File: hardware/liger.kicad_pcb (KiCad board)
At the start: 2 copper layers, 33.1 x 92.2 mm, 56 parts, among them J1 Conn_02x08_Odd_Even, Q1 Q_NPN_BEC, Q4 PMOS-DMG3413L, U1 ESP-WROOM-32, U10 EKMC1601112, U12 soft-button-4x, U2 IR-RX-TSOP34438, U3 SPH0645LM4H-B, U4 MCP73831T, U5 MAX98357AETE+T, U6 SI7020-A20, U8 TSL45315CL, U9 AP2112

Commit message: update
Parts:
- C10, C11, C5, C6, C7, C8, C9, D3, D6, Q4, R10, R11, R17, R19, R22, R9, U1, U4, U5, U9: moved to B.Cu
- moved C2 253.4 mm to (135.1, 157.5)
- moved C3 253.4 mm to (135.1, 156.0)
- moved C1 253.4 mm to (131.8, 156.0)
- moved C4 253.4 mm to (131.8, 157.5)
- moved R1 253.4 mm to (135.1, 154.5)
- moved R2 253.4 mm to (131.8, 154.5)
- moved R7 253.4 mm to (138.5, 154.5)
- moved R18 230.9 mm to (151.1, 171.9)
- moved R20 230.9 mm to (151.1, 170.4)
- moved R6 230.9 mm to (140.0, 165.1)
- moved D3 206.2 mm to (160.7, 121.6)
- moved C12 203.1 mm to (133.3, 172.1)
- moved D2 203.1 mm to (125.5, 175.8)
- moved D4 203.1 mm to (123.3, 177.4)
- moved D5 203.1 mm to (122.1, 175.8)
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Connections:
- U5 pad 10: Net-(LS1-Pad2) -> Net-(LS1-Pad1)
- U5 pad 9: Net-(LS1-Pad1) -> Net-(LS1-Pad2)
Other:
- board text added: "room sensor v0.7"
- board text removed: "room sensor v0.6"

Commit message: layout complete
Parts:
- C1, C2, C3, C4, Q1, R1, R18, R2, R20, R26, R3, R4, R5, R6, R7: moved to B.Cu
- moved R6 106.2 mm to (132.1, 59.1), turned to 270 degrees
- moved R18 104.2 mm to (147.0, 67.9), turned to 180 degrees
- moved R20 101.0 mm to (146.9, 69.5)
- moved R3 99.4 mm to (158.0, 60.7)
- moved R2 95.4 mm to (137.4, 59.2), turned to 270 degrees
- moved R5 92.6 mm to (159.3, 69.1), turned to 180 degrees
- moved R4 91.6 mm to (152.9, 68.3), turned to 90 degrees
- moved Q1 91.5 mm to (155.7, 68.3)
- moved C1 89.4 mm to (159.4, 71.0), turned to 180 degrees
- moved C2 88.3 mm to (159.4, 72.6), turned to 180 degrees
- moved C4 86.2 mm to (159.4, 75.8), turned to 180 degrees
- moved C3 85.3 mm to (159.4, 74.2), turned to 180 degrees
- moved R23 82.0 mm to (134.4, 99.4), turned to 180 degrees
- moved R26 79.3 mm to (139.8, 100.7), turned to 180 degrees
- moved D4 74.4 mm to (135.6, 104.0), turned to 270 degrees
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
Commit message: corrections
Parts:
- C12, R14, R15, R16, R23: moved to B.Cu
- moved R16 6.39 mm to (137.9, 116.5)
- moved R15 6.35 mm to (137.9, 108.8)
- moved D5 5.48 mm to (137.9, 116.5)
- moved D4 5.35 mm to (137.9, 108.8)
- moved D2 5.32 mm to (156.5, 112.9)
- moved R14 3.82 mm to (156.5, 116.7), turned to 270 degrees
- moved C12 0.62 mm to (134.1, 101.6), turned to 0 degrees
- moved U12 0.61 mm to (146.7, 88.4)
- moved R23 0.58 mm to (134.1, 99.9), turned to 0 degrees

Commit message: ws2812b
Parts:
- removed R23: R_150, Resistor_SMD:R_0603_1608Metric_Pad1.05x0.95mm_HandSolder
- added LOGO: , open-automation:pyfi_symbol, B.Cu at (163.1, 49.8)
- D7: value WS2812 -> WS2812B; footprint LED_SMD:LED_WS2812_PLCC6_5.0x5.0mm_P1.6mm -> LED_SMD:LED_WS2812B_PLCC4_5.0x5.0mm_P3.2mm
- moved C12 25.1 mm to (159.1, 100.3), turned to 180 degrees
- moved R14 0.97 mm to (157.4, 117.1), turned to 0 degrees
- moved R3 0.51 mm to (158.0, 61.2)
- moved D7 0.09 mm to (147.1, 88.6), turned to 180 degrees
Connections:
- C12 pad 2: Net-(C12-Pad2) -> /V_USB
- D7 pad 1: Net-(D7-Pad1) -> /V_USB
- D7 pad 2: /BUTTON_LED -> Net-(D7-Pad2)
- D7 pad 3: Net-(C12-Pad2) -> GND
- D7 pad 4: Net-(D7-Pad4) -> /BUTTON_LED

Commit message: pcb complete
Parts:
- moved D3 4.48 mm to (160.9, 117.1)
- moved R19 1.26 mm to (159.5, 107.4), turned to 270 degrees
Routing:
- net /3V3: track 0.00 -> 165.5 mm, vias 0 -> 14
- net /I2S_BCLK: track 0.00 -> 126.8 mm, vias 0 -> 5
- net /SCL: track 0.00 -> 83.8 mm, vias 0 -> 2
- net /SDA: track 0.00 -> 76.3 mm, vias 0 -> 2
- net /I2S_WS: track 0.00 -> 73.3 mm, vias 0 -> 7
- net /ZERO_DETECT: track 0.00 -> 62.1 mm, vias 0 -> 8
- net /V_USB: track 0.00 -> 56.1 mm, vias 0 -> 3
- net /TXD: track 0.00 -> 54.6 mm, vias 0 -> 4
- net /RXD: track 0.00 -> 53.6 mm, vias 0 -> 4
- net /IR_RX: track 0.00 -> 50.8 mm, vias 0 -> 8
- net /I2S_DATA_OUT: track 0.00 -> 46.4 mm, vias 0 -> 10
- net GND: track 0.00 -> 43.4 mm, vias 0 -> 27
- net /IR_TX: track 0.00 -> 41.9 mm, vias 0 -> 6
- net /PROG: track 0.00 -> 38.2 mm, vias 0 -> 4
- net /RELAY: track 0.00 -> 34.1 mm, vias 0 -> 7
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
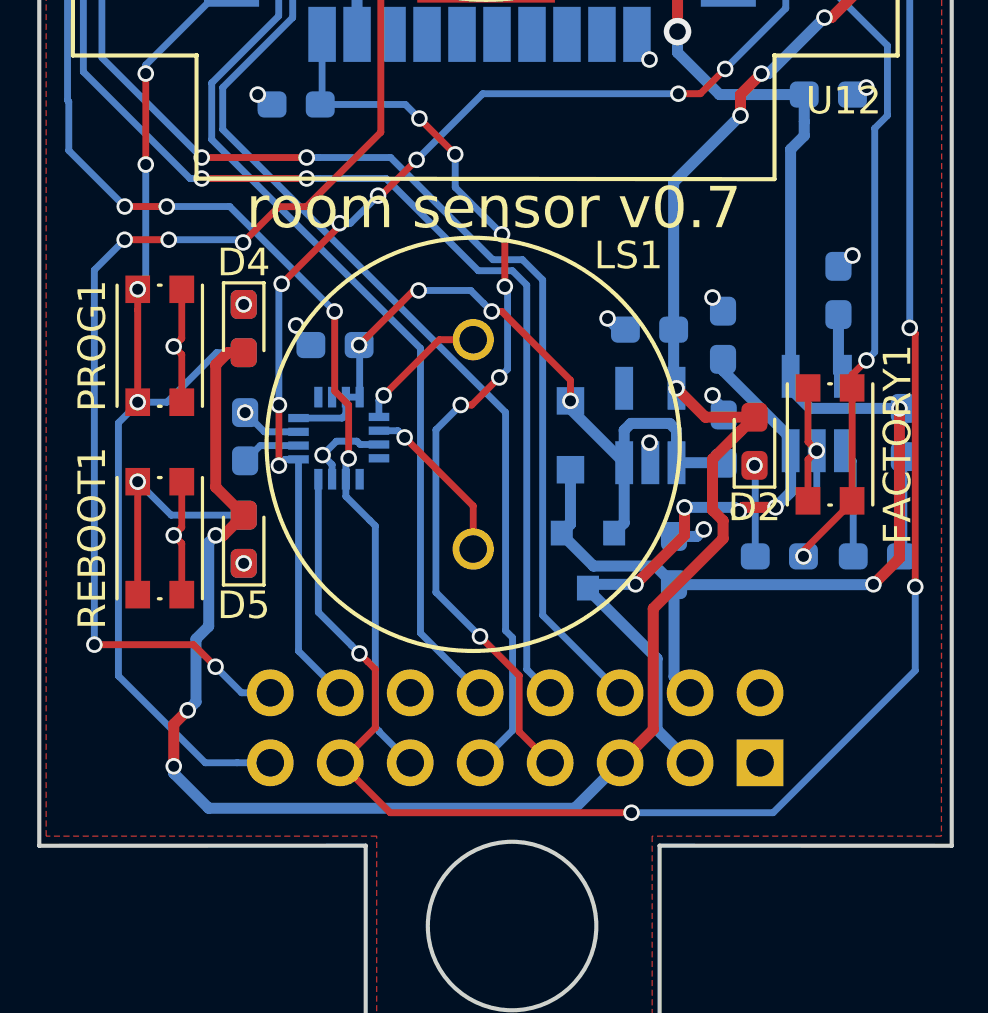
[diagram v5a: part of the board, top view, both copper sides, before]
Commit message: final touches on silkscreen, sending off to oshpark
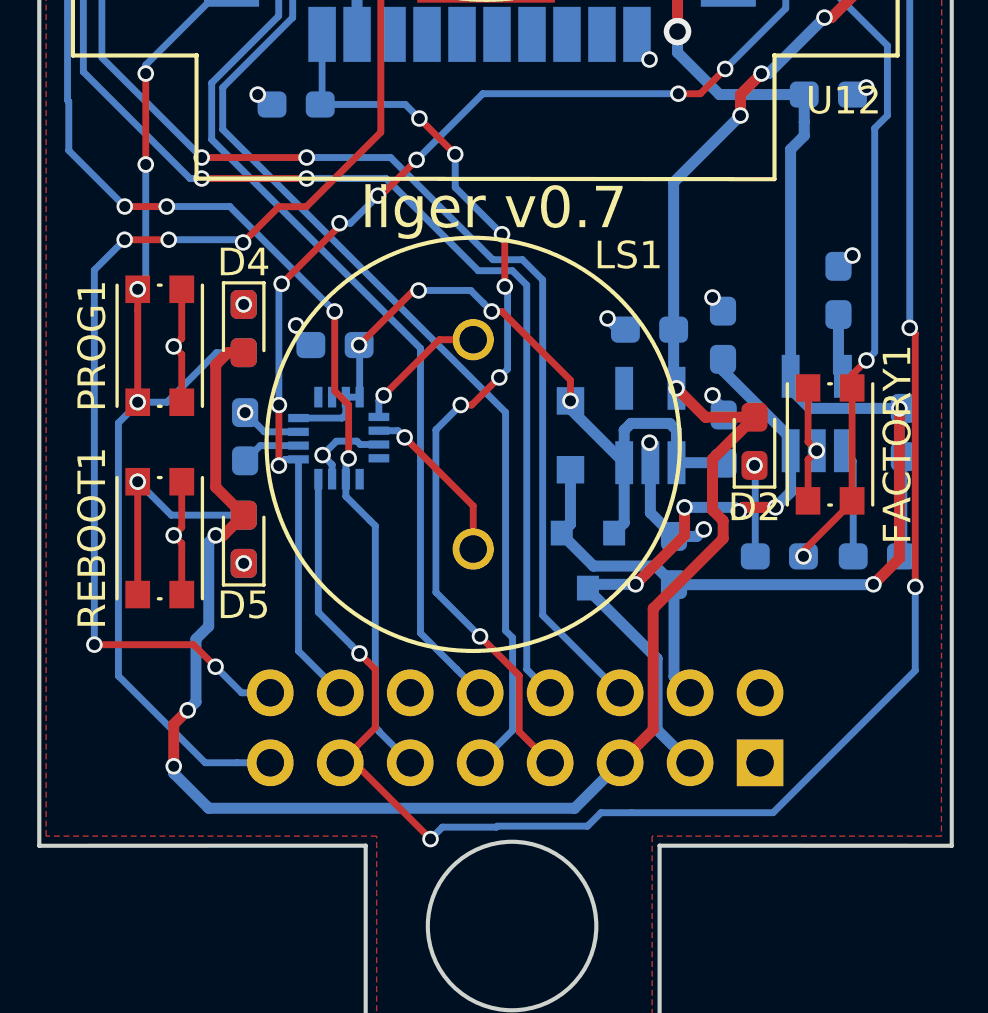
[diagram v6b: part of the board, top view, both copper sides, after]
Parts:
- moved LOGO 3.22 mm to (159.9, 50.3)
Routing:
- net GND: track 43.4 -> 44.5 mm
- net /I2S_BCLK: track 126.8 -> 127.7 mm
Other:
- board text added: "liger v0.7"
- board text removed: "room sensor v0.7"
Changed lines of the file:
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@@
-(kicad_pcb (version 20171130) (host pcbnew 5.0.0-rc3-unknown-3df2743~65~ubuntu17.10.1)
+(kicad_pcb (version 20171130) (host pcbnew 6.0.0-rc1-unknown-7a10feb~66~ubuntu18.04.1)
   (general
     (thickness 1.6)
     (drawings 57)
-    (tracks 716)
+    (tracks 723)
     (zones 0)
     (modules 56)
@@
   )
   (setup
-    (last_trace_width 0.25)
+    (last_trace_width 0.4)
     (user_trace_width 0.25)
     (user_trace_width 0.4)
@@
     (zone_45_only yes)
     (trace_min 0.2)
-    (segment_width 0.2)
-    (edge_width 0.15)
     (via_size 0.6)
     (via_drill 0.4)
@@
     (uvia_min_size 0.2)
     (uvia_min_drill 0.1)
+    (edge_width 0.15)
+    (segment_width 0.2)
     (pcb_text_width 0.3)
     (pcb_text_size 1.5 1.5)
@@
     (visible_elements FFFFFF7F)
     (pcbplotparams
-      (layerselection 0x010f0_80000001)
+      (layerselection 0x010f0_ffffffff)
       (usegerberextensions false)
       (usegerberattributes false)
@@
   )
   (module open-automation:pyfi_symbol (layer B.Cu)
-    (at 163.068 49.784 180)
+    (at 159.893 50.3428 180)
     (fp_text reference LOGO (at 0 -5 180) (layer B.SilkS) hide
       (effects (font (size 1.524 1.524) (thickness 0.3)) (justify mirror))
@@
   (gr_line (start 427.228 142.748) (end 394.2715 75.7555) (layer Dwgs.User) (width 0.15))
   (gr_line (start 427.2915 75.7555) (end 394.2715 142.748) (layer Dwgs.User) (width 0.15))
-  (gr_text "room sensor v0.7" (at 147 104.45) (layer F.SilkS)
+  (gr_text "liger v0.7" (at 147 104.45) (layer F.SilkS)
     (effects (font (size 1.5 1.5) (thickness 0.3)))
   )
@@
   (segment (start 151.779 108.8644) (end 151.5364 108.8644) (width 0.4) (layer B.Cu) (net 1))
   (segment (start 151.5364 108.8644) (end 151.13 108.458) (width 0.4) (layer B.Cu) (net 1))
-  (segment (start 158.7246 113.2586) (end 158.7246 114.7626) (width 0.25) (layer B.Cu) (net 1))
-  (segment (start 158.7246 114.7626) (end 158.4072 115.08) (width 0.25) (layer B.Cu) (net 1))
   (via (at 158.7246 113.2586) (size 0.6) (drill 0.4) (layers F.Cu B.Cu) (net 1))
   (segment (start 158.4072 110.98) (end 158.4072 112.9412) (width 0.25) (layer F.Cu) (net 1))
   (segment (start 158.4072 112.9412) (end 158.7246 113.2586) (width 0.25) (layer F.Cu) (net 1))
-  (segment (start 158.4072 113.576) (end 158.7246 113.2586) (width 0.25) (layer F.Cu) (net 1))
-  (segment (start 158.4072 115.08) (end 158.4072 113.576) (width 0.25) (layer F.Cu) (net 1))
   (segment (start 154.702 67.376) (end 154.702 67.326) (width 0.4) (layer B.Cu) (net 1))
   (via (at 154.178 66.802) (size 0.6) (drill 0.4) (layers F.Cu B.Cu) (net 1))
@@
   (segment (start 139.82501 108.88781) (end 139.82501 108.712) (width 0.25) (layer B.Cu) (net 1))
   (segment (start 140.3604 109.4232) (end 139.82501 108.88781) (width 0.25) (layer B.Cu) (net 1))
+  (segment (start 152.6832 115.5116) (end 153.543 116.3714) (width 0.4) (layer B.Cu) (net 1))
+  (segment (start 152.6832 113.6942) (end 152.6832 115.5116) (width 0.4) (layer B.Cu) (net 1))
+  (segment (start 158.4072 113.576) (end 158.7246 113.2586) (width 0.25) (layer F.Cu) (net 1))
+  (segment (start 158.4072 115.08) (end 158.4072 113.576) (width 0.25) (layer F.Cu) (net 1))
   (segment (start 156.702 64.0174) (end 156.6926 64.008) (width 0.4) (layer B.Cu) (net 2))
   (segment (start 156.702 68.326) (end 156.702 64.0174) (width 0.4) (layer B.Cu) (net 2))
@@
   (segment (start 142.424989 120.918509) (end 142.12499 120.61851) (width 0.25) (layer F.Cu) (net 39))
   (via (at 142.12499 120.61851) (size 0.6) (drill 0.4) (layers F.Cu B.Cu) (net 39))
-  (via (at 152 126.4) (size 0.6) (drill 0.4) (layers F.Cu B.Cu) (net 39))
-  (segment (start 141.4272 124.587) (end 143.2402 126.4) (width 0.25) (layer F.Cu) (net 39))
-  (segment (start 143.2402 126.4) (end 152 126.4) (width 0.25) (layer F.Cu) (net 39))
-  (via (at 162.3 118.2) (size 0.6) (drill 0.4) (layers F.Cu B.Cu) (net 39))
-  (segment (start 162.3 121.239202) (end 162.3 118.2) (width 0.25) (layer B.Cu) (net 39))
-  (segment (start 152 126.4) (end 157.139202 126.4) (width 0.25) (layer B.Cu) (net 39))
-  (segment (start 157.139202 126.4) (end 162.3 121.239202) (width 0.25) (layer B.Cu) (net 39))
-  (via (at 162.1 108.8) (size 0.6) (drill 0.4) (layers F.Cu B.Cu) (net 39))
-  (segment (start 162.3 118.2) (end 162.3 109) (width 0.25) (layer F.Cu) (net 39))
-  (segment (start 162.3 109) (end 162.1 108.8) (width 0.25) (layer F.Cu) (net 39))
-  (segment (start 162.1 94.83) (end 160.1 92.83) (width 0.25) (layer B.Cu) (net 39))
   (segment (start 162.1 108.8) (end 162.1 94.83) (width 0.25) (layer B.Cu) (net 39))
+  (segment (start 162.1 94.83) (end 160.1 92.83) (width 0.25) (layer B.Cu) (net 39))
+  (segment (start 162.3 109) (end 162.1 108.8) (width 0.25) (layer F.Cu) (net 39))
+  (segment (start 162.3 118.2) (end 162.3 109) (width 0.25) (layer F.Cu) (net 39))
+  (via (at 162.1 108.8) (size 0.6) (drill 0.4) (layers F.Cu B.Cu) (net 39))
+  (segment (start 157.139202 126.4) (end 162.3 121.239202) (width 0.25) (layer B.Cu) (net 39))
+  (segment (start 152 126.4) (end 157.139202 126.4) (width 0.25) (layer B.Cu) (net 39))
+  (segment (start 162.3 121.239202) (end 162.3 118.2) (width 0.25) (layer B.Cu) (net 39))
+  (via (at 162.3 118.2) (size 0.6) (drill 0.4) (layers F.Cu B.Cu) (net 39))
+  (segment (start 152 126.4) (end 150.8918 126.4) (width 0.25) (layer B.Cu) (net 39))
+  (segment (start 150.8918 126.4) (end 150.4038 126.888) (width 0.25) (layer B.Cu) (net 39))
+  (segment (start 141.4272 124.7798) (end 141.4272 124.587) (width 0.25) (layer F.Cu) (net 39))
+  (segment (start 147.1318 126.888) (end 147.096 126.9238) (width 0.25) (layer B.Cu) (net 39))
+  (segment (start 150.4038 126.888) (end 147.1318 126.888) (width 0.25) (layer B.Cu) (net 39))
+  (via (at 144.7038 127.3556) (size 0.6) (drill 0.4) (layers F.Cu B.Cu) (net 39))
+  (segment (start 147.096 126.9238) (end 145.1356 126.9238) (width 0.25) (layer B.Cu) (net 39))
+  (segment (start 145.1356 126.9238) (end 144.7038 127.3556) (width 0.25) (layer B.Cu) (net 39))
+  (segment (start 141.9352 124.587) (end 141.4272 124.587) (width 0.25) (layer F.Cu) (net 39))
+  (segment (start 144.7038 127.3556) (end 141.9352 124.587) (width 0.25) (layer F.Cu) (net 39))
   (segment (start 139.911 120.5308) (end 141.4272 122.047) (width 0.25) (layer B.Cu) (net 40))
   (segment (start 139.911 113.5734) (end 139.911 120.5308) (width 0.25) (layer B.Cu) (net 40))

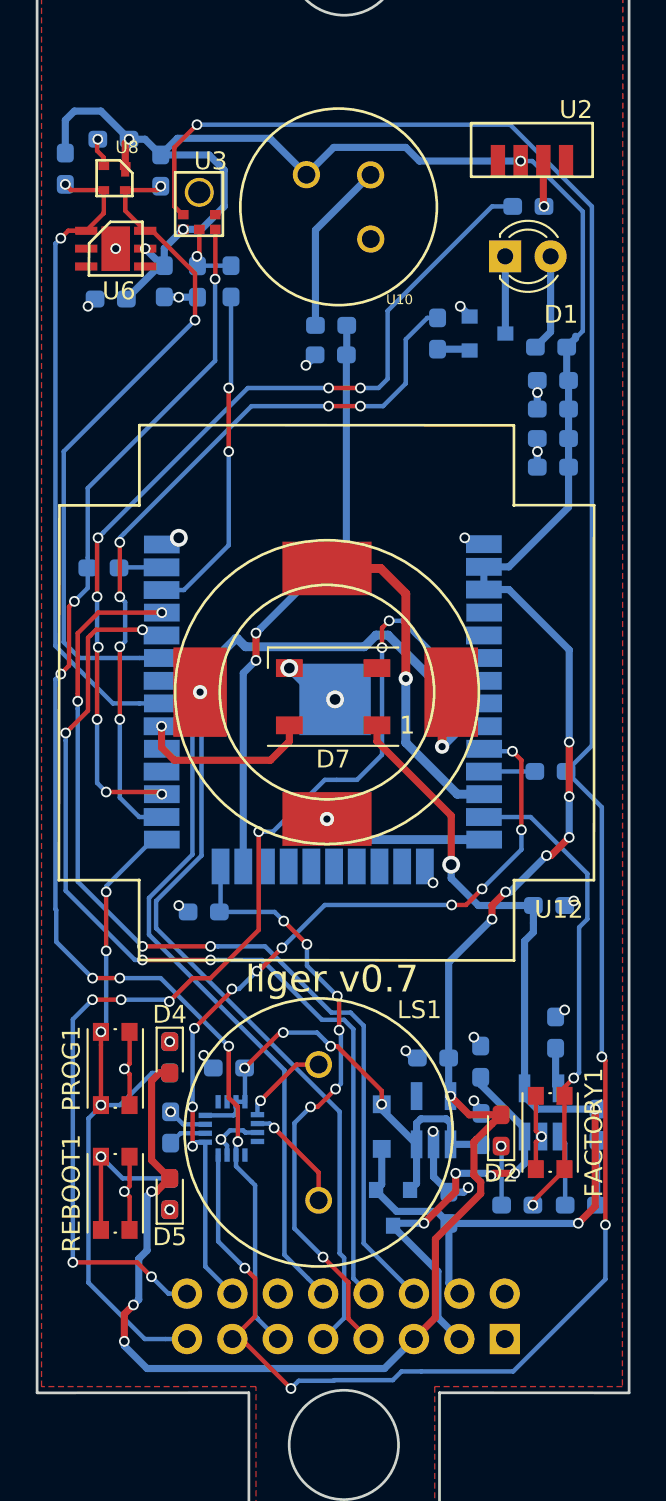
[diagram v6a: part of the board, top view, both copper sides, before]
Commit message: update schematic
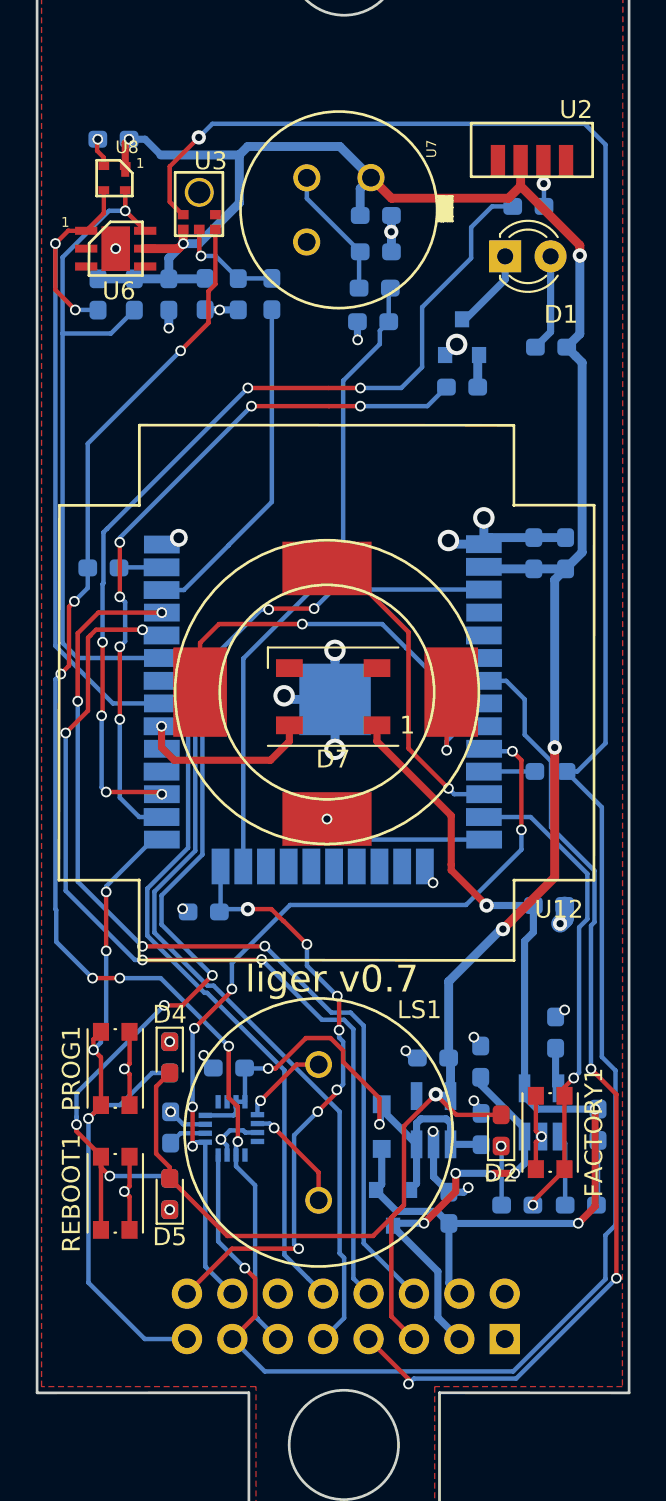
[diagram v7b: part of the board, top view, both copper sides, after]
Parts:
- removed LOGO: , open-automation:pyfi_symbol
- removed R18: R_100k, Resistor_SMD:R_0603_1608Metric_Pad1.05x0.95mm_HandSolder
- removed U10: EKMC1601112, open-automation:EKMC1601112
- added R8: R_47.5, Resistor_SMD:R_0603_1608Metric_Pad1.05x0.95mm_HandSolder, B.Cu at (149.4, 65.8)
- added U7: PYQ2898, open-automation:PYQ2898, F.Cu at (147.4, 61.4)
- C3: value C_10uF -> C_0.1uF
- C4: value C_1uF -> C_100pF
- moved C3 15.9 mm to (149.5, 61.7), turned to 0 degrees
- moved C4 15.6 mm to (149.5, 63.8), turned to 0 degrees
- moved C1 9.73 mm to (158.3, 80.6), turned to 90 degrees
- moved C2 8.10 mm to (160.1, 80.6), turned to 90 degrees
- moved R6 7.27 mm to (133.9, 66.1)
- moved R2 7.09 mm to (135.9, 66.1)
- moved R4 3.30 mm to (154.3, 71.3), turned to 180 degrees
- moved C10 3.26 mm to (137.9, 66.1), turned to 270 degrees
- moved R20 3.01 mm to (149.3, 67.7)
- moved C5 2.39 mm to (139.9, 66.1)
- moved R11 2.39 mm to (143.6, 66.1)
- moved R9 2.39 mm to (141.8, 66.1)
- moved Q1 1.44 mm to (154.3, 68.5), turned to 90 degrees
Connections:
- C4 pad 1: /3V3 -> Net-(C4-Pad1)
- J1 pad 16: /ZERO_DETECT -> /RELAY
- J1 pad 7: /RELAY -> /ZERO_DETECT
- U1 pad 3: /3V3 -> /EN
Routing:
- net /EN: track 8.45 -> 60.1 mm, vias 1 -> 6
- net /3V3: track 165.5 -> 150.8 mm, vias 14 -> 6
- net GND: track 44.5 -> 56.6 mm, vias 27 -> 28
- net Net-(R18-Pad2): track 9.70 -> 0.00 mm
- net Net-(C4-Pad1): track 0.00 -> 7.43 mm
- net /ZERO_DETECT: track 62.1 -> 54.9 mm, vias 8 -> 3
- net /I2S_BCLK: track 127.7 -> 131.2 mm, vias 5 -> 2
- net /SDA: track 76.3 -> 79.4 mm
- net /PIR: track 32.7 -> 35.8 mm, vias 2 -> 0
- net /PROG: track 38.2 -> 40.8 mm
- net /IR_TX: track 41.9 -> 39.3 mm
- net Net-(R11-Pad2): track 3.99 -> 6.06 mm
- net /V_IN: track 27.3 -> 29.1 mm, vias 4 -> 2
- net /SCL: track 83.8 -> 85.4 mm, vias 2 -> 1
- net /T_LEFT: track 19.8 -> 20.9 mm
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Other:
- board text added: "1"

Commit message: update button
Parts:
- added LOGO: , open-automation:pyfi_symbol, B.Cu at (157.2, 50.9)
- U7: footprint open-automation:PYQ2898 -> Package_TO_SOT_THT:TO-5-3
- moved C4 4.57 mm to (147.2, 59.8)
- moved C3 4.20 mm to (147.2, 58.1)
- moved U7 2.73 mm to (144.7, 61.4), turned to 0 degrees
- moved C12 1.34 mm to (158.2, 99.4), turned to 270 degrees
- moved U12 0.59 mm to (147.1, 87.9)
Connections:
- U7 pad 2: GND -> Net-(C4-Pad1)
- U7 pad 3: Net-(C4-Pad1) -> GND
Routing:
- net /3V3: track 150.8 -> 155.3 mm, vias 6 -> 7
- net GND: track 56.6 -> 60.3 mm
- net /SCL: track 85.4 -> 89.0 mm
- net /BUTTON_LED: track 9.97 -> 13.5 mm
- net /T_UP: track 17.8 -> 20.5 mm
- net /I2S_BCLK: track 131.2 -> 133.6 mm
- net /SDA: track 79.4 -> 78.1 mm
- net /I2S_WS: track 73.3 -> 74.5 mm, vias 7 -> 5
- net Net-(C4-Pad1): track 7.43 -> 6.92 mm
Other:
- board text added: "liger v0.7.1"
- board text removed: "liger v0.7"
